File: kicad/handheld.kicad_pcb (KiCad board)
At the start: 4 copper layers, 240 x 76 mm, 95 parts, among them J1 Conn_01x08, J2 61300311121, J3 AVR-PDI-6, J4 UE27AC54100, SW1 HOLD, SW2 PAUSE, SW3 SDROP, SW4 HDROP, SW5 ROTR, SW6 RIGHT, SW7 ROTL, SW8 RIGHT, U1 TFBS4711, U10 DMN601, U11 NSI45015, U12 SN54LV574, U13 P-FET, U14 NSI45015, U15 DMN601, U16 NSI45015, U17 NSI45015, U18 DMN601, U19 P-FET, U2 ATxmega64C3-AU, U20 NSI45015, U21 74HCT595, U22 NSI45015, U23 DMN601, U24 NSI45015, U25 P-FET, U26 NSI45015, U27 DMN601, U28 NSI45015, U29 SN54LV574, U3 P-FET, U30 NSI45015, U31 DMN601, U32 NSI45015, U33 P-FET, U34 NSI45015, U35 DMN601, U36 NSI45015, U37 NSI45015, U38 P-FET, U39 DMN601, U4 LM3671MF-3.3, U40 NSI45015, U41 NSI45015, U42 DMN601, U43 NSI45015, U44 SN54LV574, U45 74HCT595, U46 P-FET, U47 NSI45015, U48 DMN601, U49 NSI45015, U5 NSI45015, U50 NSI45015, U51 DMN601, U52 P-FET, U53 NSI45015, U6 P-FET, U7 DMN601, U8 NSI45015, U9 NSI45015

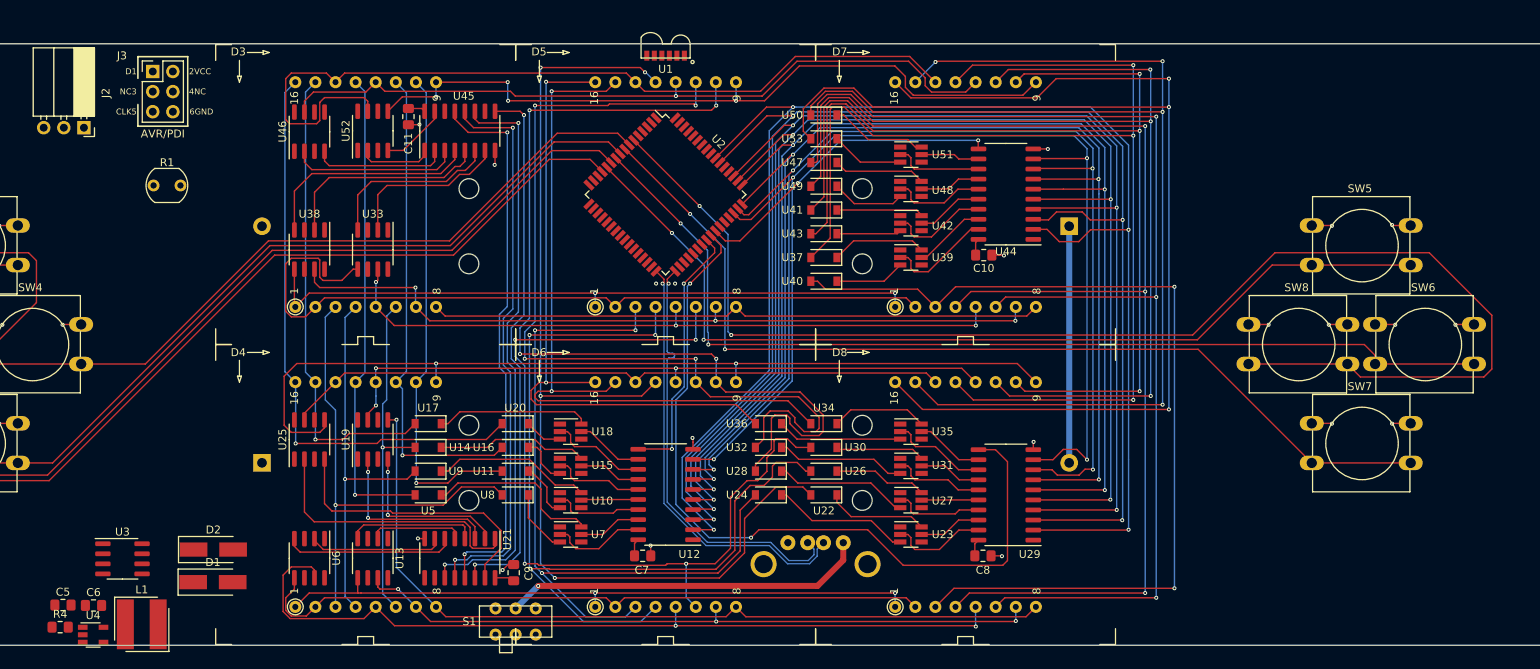
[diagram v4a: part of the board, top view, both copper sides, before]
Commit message: Added power plane and reassigned pinout
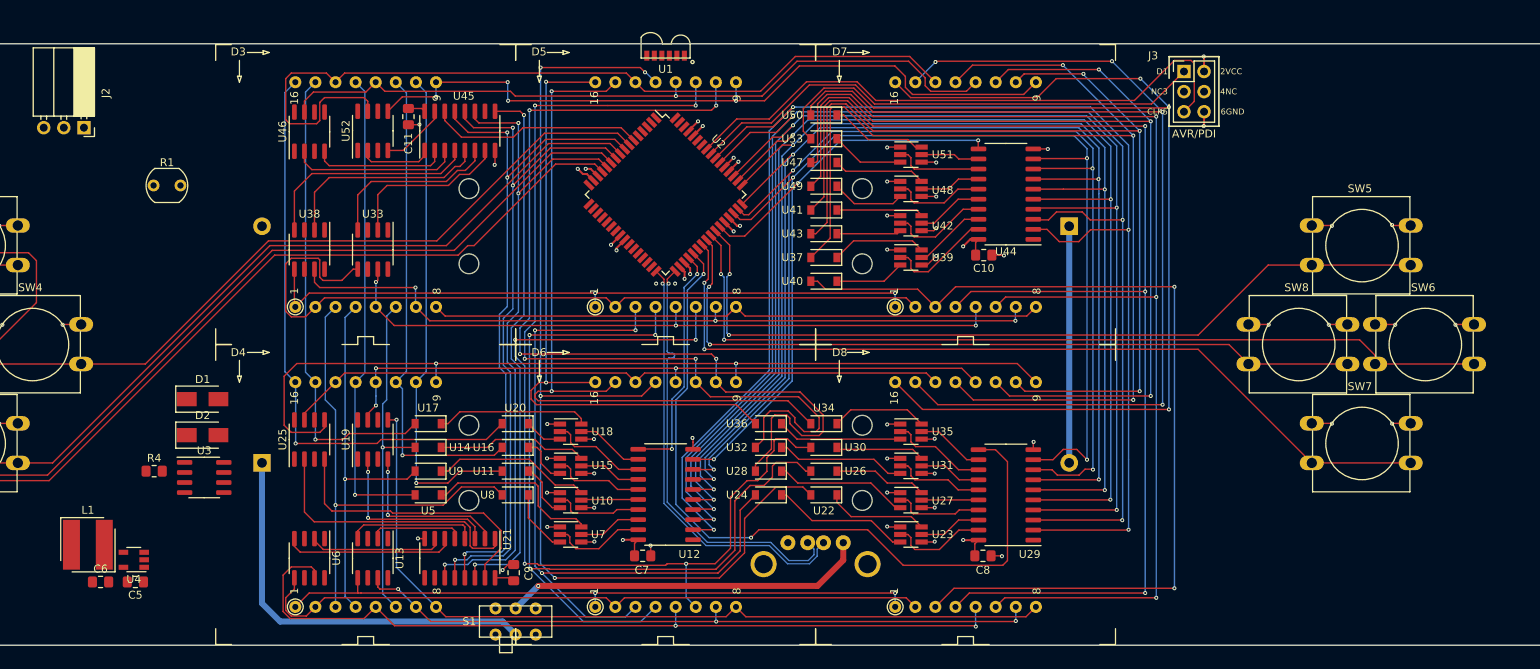
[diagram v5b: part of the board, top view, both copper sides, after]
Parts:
- D1, D2: value MRA4007 -> MRA4003T3G; footprint Diode_SMD:D_SMA_Handsoldering -> Diode_SMD:D_SMA
- moved J3 130.3 mm to (217.9, 67.1)
- moved D1 23.2 mm to (93.9, 108.5)
- moved R4 23.0 mm to (87.8, 117.6)
- moved U3 14.6 mm to (94.1, 118.4)
- moved D2 14.5 mm to (93.9, 113.0)
- moved L1 12.1 mm to (79.4, 126.9)
- moved U4 10.8 mm to (85.2, 128.8), turned to 180 degrees
- moved C5 9.60 mm to (85.4, 131.6), turned to 180 degrees
- moved C6 3.10 mm to (81.0, 131.6)
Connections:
- net Net-(U1-Pad2) renamed /IrTX
- net Net-(U1-Pad3) renamed /IrRX
- D2 pad 1: Net-(D2-Pad1) -> U_PWR
- D2 pad 2: U_PWR -> Net-(D2-Pad2)
- R4 pad 1: Net-(D2-Pad1) -> Net-(D2-Pad2)
- S1 pad 1: Net-(D1-Pad1) -> Net-(D1-Pad2)
- S1 pad 4: Net-(D2-Pad1) -> Net-(D2-Pad2)
- U12 pad 1: /Matrix Driver/~OE -> /~OE
- U2 pad 10: Net-(SW6-Pad2) -> /LE
- U2 pad 12: Net-(SW5-Pad2) -> /ROWCLK
- U2 pad 36: /Matrix Driver/ROWCLK -> /Matrix Driver/SEGCLK0
- U2 pad 37: /Matrix Driver/ROWSDI -> /Matrix Driver/SEGCLK1
- U2 pad 38: /Matrix Driver/LE -> Net-(U2-Pad38)
- U2 pad 39: /Matrix Driver/~OE -> Net-(SW7-Pad2)
- U2 pad 40: /Matrix Driver/SEGCLK0 -> Net-(SW8-Pad2)
- U2 pad 41: /Matrix Driver/SEGCLK1 -> Net-(SW6-Pad2)
- U2 pad 42: /Matrix Driver/SEGCLK2 -> Net-(SW5-Pad2)
- U2 pad 43: Net-(U2-Pad43) -> /Matrix Driver/SEGCLK2
- U2 pad 6: Net-(SW8-Pad2) -> /ROWSDI
- U2 pad 8: Net-(SW7-Pad2) -> /~OE
- U21 pad 11: /Matrix Driver/ROWCLK -> /ROWCLK
- U21 pad 12: /Matrix Driver/LE -> /LE
- U21 pad 13: /Matrix Driver/~OE -> /~OE
- U29 pad 1: /Matrix Driver/~OE -> /~OE
- U3 pad 1: Net-(D1-Pad2) -> Net-(D1-Pad1)
- U3 pad 2: Net-(D2-Pad1) -> Net-(D2-Pad2)
- U44 pad 1: /Matrix Driver/~OE -> /~OE
- U45 pad 11: /Matrix Driver/ROWCLK -> /ROWCLK
- U45 pad 12: /Matrix Driver/LE -> /LE
- U45 pad 13: /Matrix Driver/~OE -> /~OE
- U45 pad 14: /Matrix Driver/ROWSDI -> /ROWSDI
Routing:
- net /~OE: track 0.00 -> 87.5 mm, vias 0 -> 3
- net /LE: track 0.00 -> 86.9 mm, vias 0 -> 3
- net /ROWCLK: track 0.00 -> 86.5 mm, vias 0 -> 3
- net Net-(SW8-Pad2): track 172.1 -> 95.5 mm
- net Net-(J3-Pad5): track 0.00 -> 75.0 mm
- net /Matrix Driver/ROWCLK: track 73.0 -> 0.00 mm, vias 2 -> 0
- net /Matrix Driver/LE: track 71.4 -> 0.00 mm, vias 2 -> 0
- net /Matrix Driver/~OE: track 70.1 -> 0.00 mm, vias 2 -> 0
- net Net-(J3-Pad1): track 0.00 -> 66.1 mm
- net GND: track 53.8 -> 107.2 mm, vias 28 -> 59
- net /power/6V: track 0.00 -> 51.4 mm
- net /ROWSDI: track 0.00 -> 27.1 mm
- net VDD: track 6.54 -> 26.1 mm, vias 0 -> 10
- net Net-(SW6-Pad2): track 126.8 -> 110.5 mm
- net Net-(SW5-Pad2): track 120.2 -> 104.0 mm
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- added copper zone on In2.Cu.Pwr, net VDD
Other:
- net class VDD added: clearance 0.254, trace_width 0.1778, via_dia 0.508, via_drill 0.254

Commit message: Wired up buzzer and LDR
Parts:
- S1: moved to B.Cu
- moved C1 186.6 mm to (128.1, 57.4)
- moved C3 186.6 mm to (132.8, 57.4)
- moved C4 186.6 mm to (137.6, 57.4)
- moved R2 186.6 mm to (156.6, 57.4)
- moved RV1 186.6 mm to (147.1, 57.4)
- moved C2 186.6 mm to (112.4, 46.5)
- moved R1 151.6 mm to (238.7, 67.7)
- moved RV2 109.3 mm to (216.5, 80.3), turned to 180 degrees
- moved R3 100.9 mm to (240.4, 71.5), turned to 180 degrees
- moved BZ1 26.6 mm to (216.5, 68.7)
- moved J3 10.2 mm to (228.1, 67.8)
- turned S1 to 180 degrees
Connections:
- S1 pad 1: Net-(D1-Pad2) -> Net-(S1-Pad1)
- S1 pad 3: Net-(S1-Pad3) -> Net-(D1-Pad2)
- S1 pad 4: Net-(D2-Pad2) -> Net-(S1-Pad4)
- S1 pad 6: Net-(S1-Pad6) -> Net-(D2-Pad2)
- U2 pad 10: /LE -> Net-(U2-Pad10)
- U2 pad 11: Net-(SW2-Pad2) -> Net-(U2-Pad11)
- U2 pad 12: /ROWCLK -> Net-(U2-Pad12)
- U2 pad 13: Net-(SW1-Pad2) -> Net-(U2-Pad13)
- U2 pad 20: Net-(U2-Pad20) -> /ROWSDI
- U2 pad 21: Net-(J1-Pad6) -> /~OE
- U2 pad 22: Net-(J1-Pad7) -> /LE
- U2 pad 23: Net-(J1-Pad8) -> /ROWCLK
- U2 pad 26: Net-(RV2-Pad3) -> Net-(SW2-Pad2)
- U2 pad 27: Net-(U2-Pad27) -> Net-(SW1-Pad2)
- U2 pad 3: Net-(J1-Pad3) -> Net-(U2-Pad3)
- U2 pad 30: Net-(U2-Pad30) -> Net-(SW4-Pad2)
- U2 pad 31: Net-(U2-Pad31) -> Net-(SW3-Pad2)
- U2 pad 4: Net-(J1-Pad4) -> Net-(U2-Pad4)
- U2 pad 5: Net-(J1-Pad5) -> Net-(U2-Pad5)
- U2 pad 6: /ROWSDI -> Net-(U2-Pad6)
- U2 pad 62: Net-(U2-Pad62) -> Net-(RV2-Pad3)
- U2 pad 7: Net-(SW4-Pad2) -> Net-(U2-Pad7)
- U2 pad 8: /~OE -> Net-(U2-Pad8)
- U2 pad 9: Net-(SW3-Pad2) -> Net-(U2-Pad9)
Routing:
- net Net-(RV2-Pad3): track 0.00 -> 107.3 mm
- net Net-(R1-Pad1): track 0.00 -> 95.2 mm
- net Net-(SW1-Pad2): track 190.1 -> 106.1 mm
- net Net-(SW2-Pad2): track 154.9 -> 92.6 mm
- net GND: track 107.2 -> 69.2 mm, vias 59 -> 44
- net Net-(J3-Pad1): track 66.1 -> 83.8 mm
- net /ROWSDI: track 27.1 -> 35.1 mm, vias 0 -> 2
- net Net-(BZ1-Pad2): track 0.00 -> 7.20 mm
- net /Matrix Driver/COL20: track 155.0 -> 148.7 mm
- net /Matrix Driver/COL16: track 143.5 -> 149.4 mm
- net /Matrix Driver/COL18: track 164.4 -> 159.4 mm
- net /Matrix Driver/COL19: track 126.4 -> 131.4 mm
- net /Matrix Driver/COL21: track 132.1 -> 136.2 mm
- net /~OE: track 87.5 -> 83.6 mm
- net /Matrix Driver/COL22: track 152.0 -> 154.7 mm
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
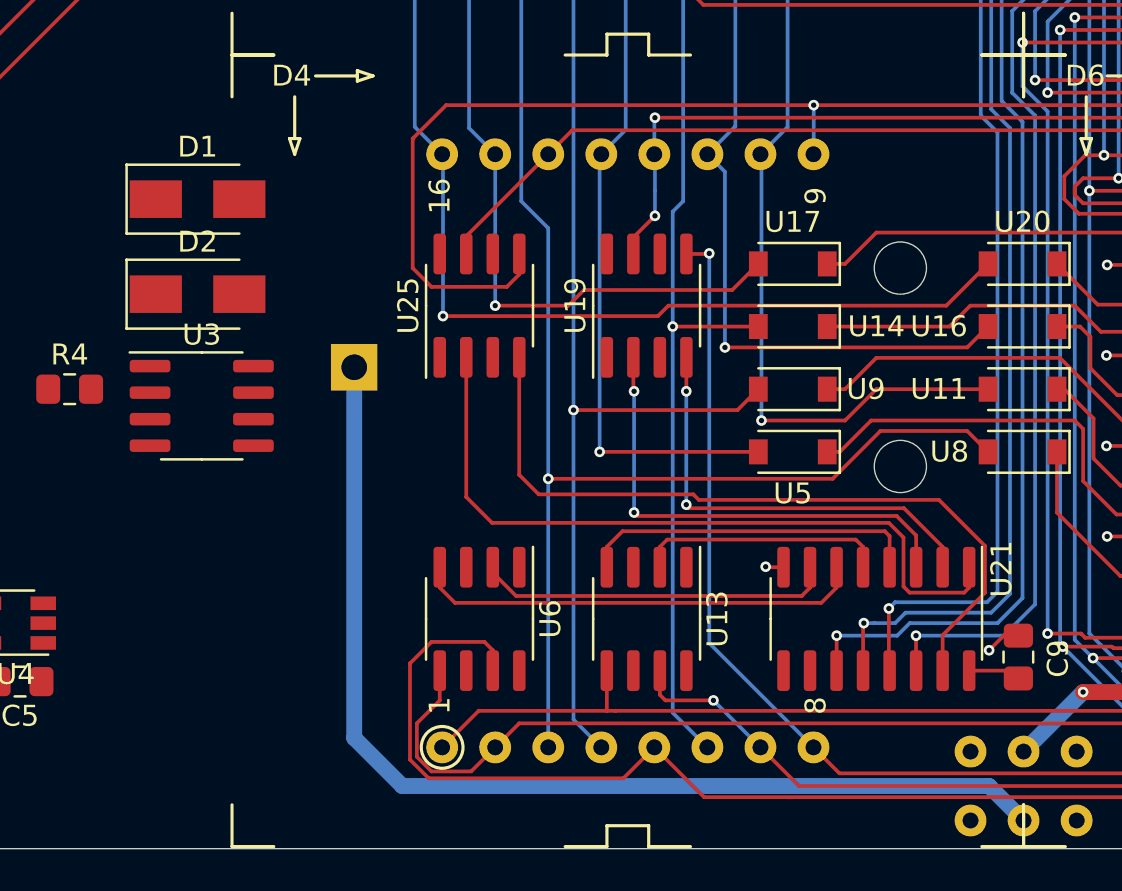
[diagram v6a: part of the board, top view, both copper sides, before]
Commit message: Places rectifiers
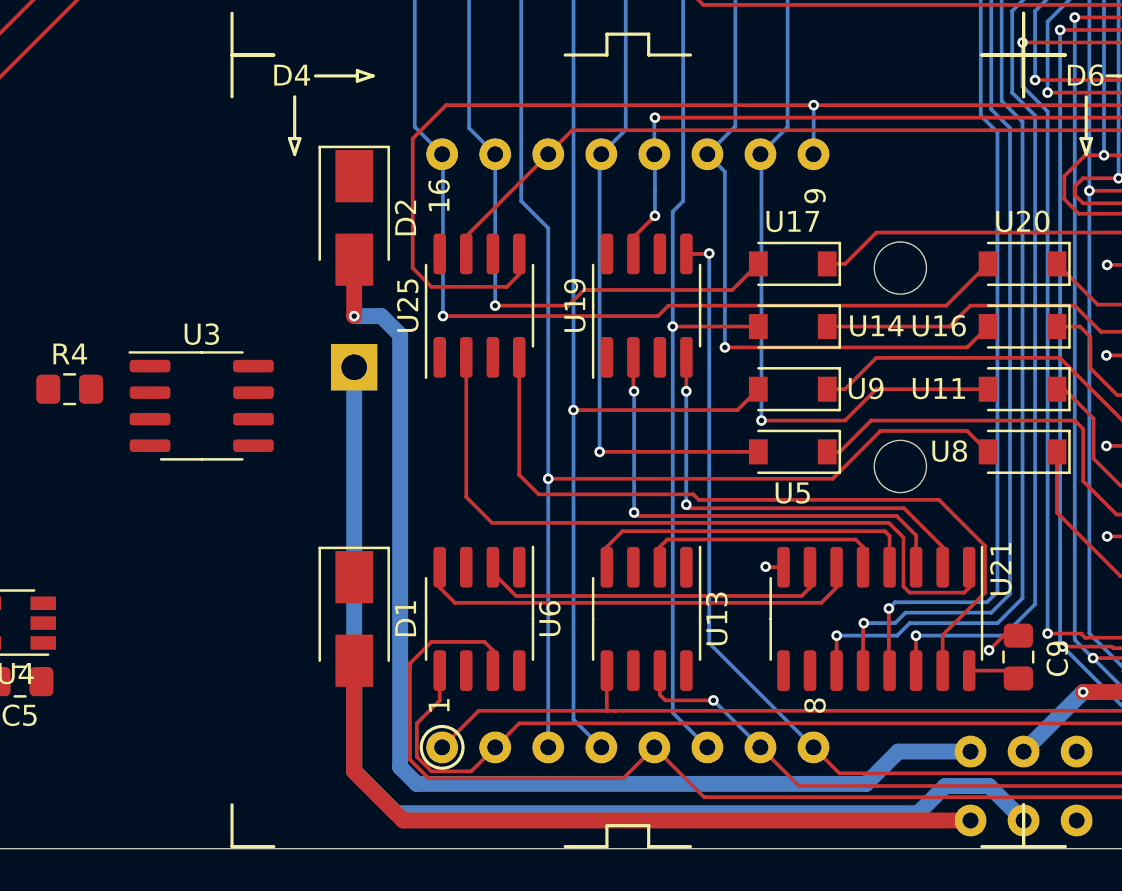
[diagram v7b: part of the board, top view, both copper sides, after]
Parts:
- moved D1 21.5 mm to (101.4, 128.6), turned to 270 degrees
- moved D2 8.34 mm to (101.4, 109.4), turned to 270 degrees
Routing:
- net Net-(D2-Pad2): track 0.00 -> 54.3 mm, vias 0 -> 1
- net Net-(D1-Pad2): track 0.00 -> 35.8 mm
- net /power/6V: track 51.4 -> 53.5 mm
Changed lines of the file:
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@@
     (thickness 1.6002)
     (drawings 4)
-    (tracks 1617)
+    (tracks 1631)
     (zones 0)
     (modules 95)
@@
   )
   (setup
-    (last_trace_width 0.1778)
+    (last_trace_width 0.762)
     (user_trace_width 0.254)
     (user_trace_width 0.508)
@@
   )
   (module Diode_SMD:D_SMA (layer Front)
-    (at 93.9 113.05)
+    (at 101.4 109.4 270)
     (descr "Diode SMA (DO-214AC)")
     (tags "Diode SMA (DO-214AC)")
     (attr smd)
-    (fp_text reference D2 (at 0 -2.5) (layer F.SilkS)
+    (fp_text reference D2 (at 0 -2.5 90) (layer F.SilkS)
       (effects (font (size 1 1) (thickness 0.15)))
     )
-    (fp_text value MRA4003T3G (at 0 2.6) (layer F.Fab)
+    (fp_text value MRA4003T3G (at 0 2.6 90) (layer F.Fab)
       (effects (font (size 1 1) (thickness 0.15)))
     )
-    (fp_text user %R (at 0 -2.5) (layer F.Fab)
+    (fp_text user %R (at 0 -2.5 90) (layer F.Fab)
       (effects (font (size 1 1) (thickness 0.15)))
     )
@@
     (fp_line (start -3.4 1.65) (end 2 1.65) (layer F.SilkS) (width 0.12))
     (fp_line (start -3.4 -1.65) (end 2 -1.65) (layer F.SilkS) (width 0.12))
-    (pad 2 smd rect (at 2 0) (size 2.5 1.8) (layers Front F.Paste F.Mask)
+    (pad 2 smd rect (at 2 0 270) (size 2.5 1.8) (layers Front F.Paste F.Mask)
       (net 178 "Net-(D2-Pad2)"))
-    (pad 1 smd rect (at -2 0) (size 2.5 1.8) (layers Front F.Paste F.Mask)
+    (pad 1 smd rect (at -2 0 270) (size 2.5 1.8) (layers Front F.Paste F.Mask)
       (net 6 U_PWR))
     (model ${KISYS3DMOD}/Diode_SMD.3dshapes/D_SMA.wrl
@@
   )
   (module Diode_SMD:D_SMA (layer Front)
-    (at 93.9 108.5)
+    (at 101.4 128.6 270)
     (descr "Diode SMA (DO-214AC)")
     (tags "Diode SMA (DO-214AC)")
     (attr smd)
-    (fp_text reference D1 (at 0 -2.5) (layer F.SilkS)
+    (fp_text reference D1 (at 0 -2.5 90) (layer F.SilkS)
       (effects (font (size 1 1) (thickness 0.15)))
     )
-    (fp_text value MRA4003T3G (at 0 2.6) (layer F.Fab)
+    (fp_text value MRA4003T3G (at 0 2.6 90) (layer F.Fab)
       (effects (font (size 1 1) (thickness 0.15)))
     )
-    (fp_text user %R (at 0 -2.5) (layer F.Fab)
+    (fp_text user %R (at 0 -2.5 90) (layer F.Fab)
       (effects (font (size 1 1) (thickness 0.15)))
     )
@@
     (fp_line (start -3.4 1.65) (end 2 1.65) (layer F.SilkS) (width 0.12))
     (fp_line (start -3.4 -1.65) (end 2 -1.65) (layer F.SilkS) (width 0.12))
-    (pad 2 smd rect (at 2 0) (size 2.5 1.8) (layers Front F.Paste F.Mask)
+    (pad 2 smd rect (at 2 0 270) (size 2.5 1.8) (layers Front F.Paste F.Mask)
       (net 8 "Net-(D1-Pad2)"))
-    (pad 1 smd rect (at -2 0) (size 2.5 1.8) (layers Front F.Paste F.Mask)
+    (pad 1 smd rect (at -2 0 270) (size 2.5 1.8) (layers Front F.Paste F.Mask)
       (net 9 "Net-(D1-Pad1)"))
     (model ${KISYS3DMOD}/Diode_SMD.3dshapes/D_SMA.wrl
@@
   (gr_line (start 32.4 63.6) (end 272.4 63.6) (layer Edge.Cuts) (width 0.05))
   (segment (start 203.4 86.65) (end 203.4 116.55) (width 0.762) (layer Back) (net 1))
+  (segment (start 128.4 137.9) (end 129.7 136.6) (width 0.762) (layer Back) (net 2))
   (segment (start 131.7988 136.6) (end 133.45 138.2512) (width 0.762) (layer Back) (net 2))
-  (segment (start 103.7 136.6) (end 131.7988 136.6) (width 0.762) (layer Back) (net 2))
-  (segment (start 101.4 134.3) (end 103.7 136.6) (width 0.762) (layer Back) (net 2))
-  (segment (start 101.4 116.55) (end 101.4 134.3) (width 0.762) (layer Back) (net 2))
+  (segment (start 129.7 136.6) (end 131.7988 136.6) (width 0.762) (layer Back) (net 2))
+  (segment (start 101.4 116.55) (end 101.4 135.9) (width 0.762) (layer Back) (net 2))
+  (segment (start 103.4 137.9) (end 128.4 137.9) (width 0.762) (layer Back) (net 2))
+  (segment (start 101.4 135.9) (end 103.4 137.9) (width 0.762) (layer Back) (net 2))
   (via (at 121.1 126.1) (size 0.508) (drill 0.254) (layers Front Back) (net 3))
   (segment (start 121.125 126.125) (end 121.1 126.1) (width 0.1778) (layer Front) (net 3))
@@
   (segment (start 155.5 91.97254) (end 155.5 92.700002) (width 0.254) (layer Front) (net 7))
   (segment (start 154.733452 91.205992) (end 155.5 91.97254) (width 0.254) (layer Front) (net 7))
+  (segment (start 101.4 135.9) (end 101.4 130.6) (width 0.762) (layer Front) (net 8))
+  (segment (start 103.7512 138.2512) (end 101.4 135.9) (width 0.762) (layer Front) (net 8))
+  (segment (start 130.91 138.2512) (end 103.7512 138.2512) (width 0.762) (layer Front) (net 8))
   (segment (start 149.696546 71.996546) (end 135.203454 71.996546) (width 0.1778) (layer Front) (net 38))
   (segment (start 158.203454 71.996546) (end 155.096546 71.996546) (width 0.1778) (layer Front) (net 38))
@@
   (segment (start 176.25 83.8) (end 181.133333 83.8) (width 0.1778) (layer Front) (net 175))
   (segment (start 174.05 81.6) (end 176.25 83.8) (width 0.1778) (layer Front) (net 175))
+  (via (at 101.4 114.1) (size 0.508) (drill 0.254) (layers Front Back) (net 178))
+  (segment (start 101.4 114.1) (end 101.4 111.4) (width 0.762) (layer Front) (net 178))
+  (segment (start 103.6 115) (end 102.7 114.1) (width 0.762) (layer Back) (net 178))
+  (segment (start 103.6 135.7) (end 103.6 115) (width 0.762) (layer Back) (net 178))
+  (segment (start 102.7 114.1) (end 101.4 114.1) (width 0.762) (layer Back) (net 178))
+  (segment (start 104.4 136.5) (end 103.6 135.7) (width 0.762) (layer Back) (net 178))
+  (segment (start 125.9 136.5) (end 104.4 136.5) (width 0.762) (layer Back) (net 178))
+  (segment (start 127.4488 134.9512) (end 125.9 136.5) (width 0.762) (layer Back) (net 178))
+  (segment (start 130.91 134.9512) (end 127.4488 134.9512) (width 0.762) (layer Back) (net 178))
   (segment (start 133.8 82.5) (end 133.8 73.6) (width 0.1778) (layer Back) (net 180))
   (via (at 133.8 89.9) (size 0.508) (drill 0.254) (layers Front Back) (net 180))
